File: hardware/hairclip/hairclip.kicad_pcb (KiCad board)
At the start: 2 copper layers, 18 parts, among them J1 Conn_Coaxial_Small, J2 Conn_ARM_SWD_TagConnect_TC2030, U1 NRF52840-CKAA-R, U2 MIC5365-3.3YD5, X1 32MHz, X2 32kHz768

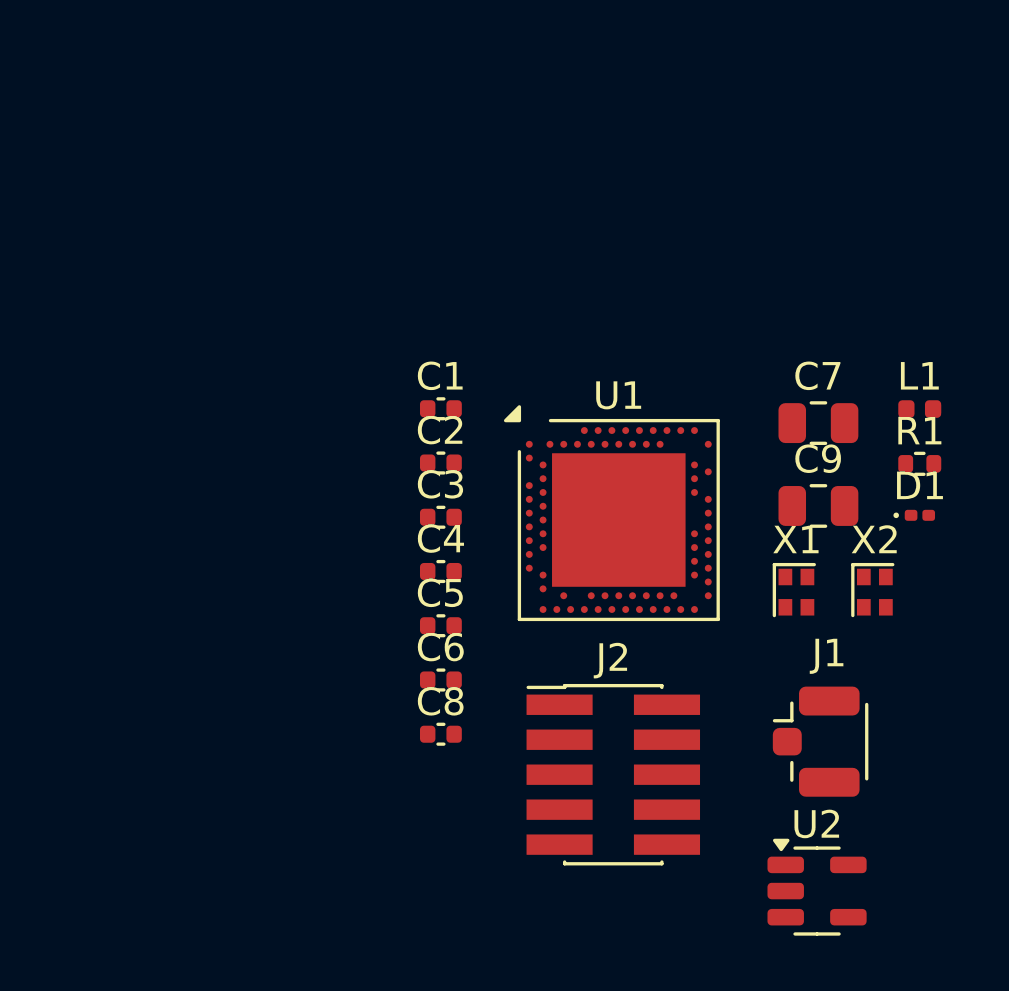
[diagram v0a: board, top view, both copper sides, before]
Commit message: add readme images
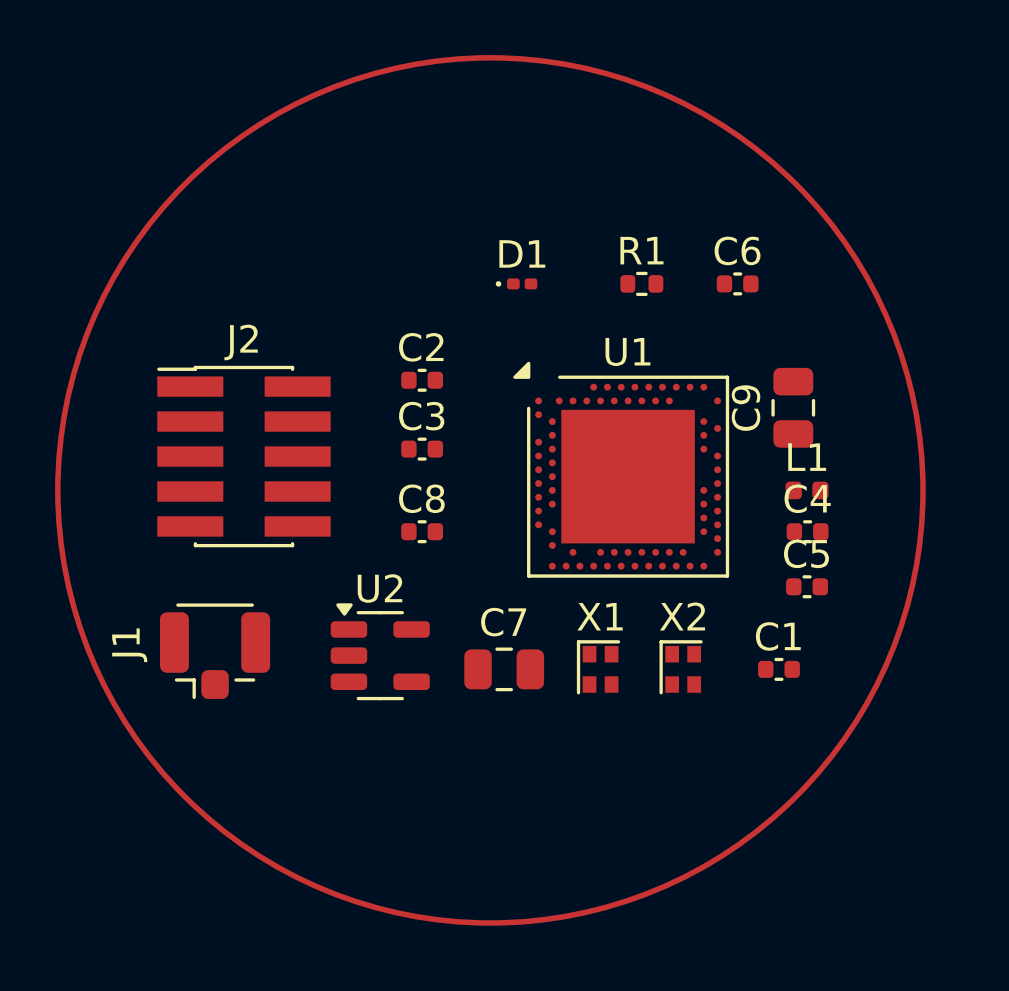
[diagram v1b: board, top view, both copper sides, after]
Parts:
- moved J1 22.1 mm to (119.0, 85.0), turned to 90 degrees
- moved U2 18.0 mm to (125.0, 85.0)
- moved C6 18.0 mm to (138.0, 71.5)
- moved J2 17.7 mm to (120.0, 77.8)
- moved D1 16.7 mm to (130.2, 71.5)
- moved C1 15.5 mm to (139.5, 85.5)
- moved C7 14.5 mm to (129.5, 85.5)
- moved C4 13.4 mm to (140.5, 80.5)
- moved C5 13.4 mm to (140.5, 82.5)
- moved R1 12.0 mm to (134.5, 71.5)
- moved X1 7.65 mm to (133.0, 85.5)
- moved X2 7.51 mm to (136.0, 85.5)
- moved C8 7.39 mm to (126.5, 80.5)
- moved L1 5.05 mm to (140.5, 79.0)
- moved C9 3.68 mm to (140.0, 76.0), turned to 90 degrees
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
